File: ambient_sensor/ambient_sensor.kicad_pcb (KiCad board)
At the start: 2 copper layers, 69.5 x 54 mm, 25 parts, among them J1 Conn_01x02_Pin, J3 Conn_01x05_Pin, J4 Conn_01x01_Pin, J5 Conn_01x04_Pin, J6 Conn_01x02_Pin, U4 ATmega328-P, U6 LD1117S33TR_SOT223, Y1 Crystal

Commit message: no more errors
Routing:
- net +5V: track 223.2 -> 217.9 mm, vias 2 -> 3
- net unconnected-(U7-3V3-Pad2)_1: track 0.00 -> 2.50 mm
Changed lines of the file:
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@@
 	(net 30 "/MISO")
 	(net 31 "/DT")
-	(net 32 "unconnected-(U7-3V3-Pad2)")
-	(net 33 "unconnected-(U7-3V3-Pad2)_1")
-	(net 34 "unconnected-(U2-3V0-Pad4)")
-	(net 35 "unconnected-(U5-CTS-Pad2)")
+	(net 32 "unconnected-(U7-3V3-Pad2)_1")
+	(net 33 "unconnected-(U2-3V0-Pad4)")
+	(net 34 "unconnected-(U5-CTS-Pad2)")
 	(footprint "Resistor_SMD:R_1206_3216Metric"
 		(layer "F.Cu")
@@
 			(layers "*.Cu" "*.Mask")
 			(remove_unused_layers no)
-			(net 35 "unconnected-(U5-CTS-Pad2)")
+			(net 34 "unconnected-(U5-CTS-Pad2)")
 			(pinfunction "CTS")
 			(pintype "input")
@@
 			)
 		)
-		(fp_text user "MISO"
-			(at -37 -18.94144 0)
+		(fp_text user "Warning: unkown dimensions "
+			(at -7 -20 0)
 			(unlocked yes)
 			(layer "User.1")
 			(effects
 				(font
-					(size 0.93472 0.93472)
-					(thickness 0.08128)
+					(size 1 1)
+					(thickness 0.1)
 				)
 				(justify right bottom)
 			)
 		)
-		(fp_text user "3V3"
-			(at -37.801187 -6.24144 0)
+		(fp_text user "5V"
+			(at -38.691397 -8.78144 0)
 			(unlocked yes)
 			(layer "User.1")
@@
 			)
 		)
-		(fp_text user "GND"
-			(at -37.534126 -21.48144 0)
+		(fp_text user "SCK"
+			(at -37.623146 -16.40144 0)
 			(unlocked yes)
 			(layer "User.1")
@@
 			)
 		)
-		(fp_text user "MOSI"
-			(at -37 -13.86144 0)
+		(fp_text user "MISO"
+			(at -37 -18.94144 0)
 			(unlocked yes)
 			(layer "User.1")
@@
 			)
 		)
-		(fp_text user "GND"
-			(at -37.623146 -3.70144 0)
+		(fp_text user "3V3"
+			(at -37.801187 -6.24144 0)
 			(unlocked yes)
 			(layer "User.1")
@@
 			)
 		)
-		(fp_text user "5V"
-			(at -38.691397 -8.78144 0)
+		(fp_text user "MOSI"
+			(at -37 -13.86144 0)
 			(unlocked yes)
 			(layer "User.1")
@@
 			)
 		)
-		(fp_text user "Warning: unkown dimensions "
-			(at -7 -20 0)
+		(fp_text user "GND"
+			(at -37.534126 -21.48144 0)
 			(unlocked yes)
 			(layer "User.1")
 			(effects
 				(font
-					(size 1 1)
-					(thickness 0.1)
+					(size 0.93472 0.93472)
+					(thickness 0.08128)
 				)
 				(justify right bottom)
 			)
 		)
-		(fp_text user "CS"
-			(at -38.557866 -11.32144 0)
+		(fp_text user "GND"
+			(at -37.623146 -3.70144 0)
 			(unlocked yes)
 			(layer "User.1")
@@
 			)
 		)
-		(fp_text user "SCK"
-			(at -37.623146 -16.40144 0)
+		(fp_text user "CS"
+			(at -38.557866 -11.32144 0)
 			(unlocked yes)
 			(layer "User.1")
@@
 			(layer "User.4")
 			(pts
-				(xy 225.25 139.25) (xy 225.25 146.5)
+				(xy 226.611 119.979) (xy 226.611 137.759)
 			)
-			(height 23)
-			(gr_text "7.2500 mm"
-				(at 201.15 142.875 90)
+			(height 7.861)
+			(gr_text "17.7800 mm"
+				(at 217.6 128.869 90)
 				(layer "User.4")
 				(effects
 					(font
 						(size 1 1)
-						(thickness 0.1)
+						(thickness 0.15)
 					)
 				)
@@
 			(layer "User.4")
 			(pts
-				(xy 226.611 119.979) (xy 229.111 119.979)
+				(xy 225.25 139.25) (xy 225.25 146.5)
 			)
-			(height -13.479)
-			(gr_text "2.5000 mm"
-				(at 227.861 105.4 0)
+			(height 23)
+			(gr_text "7.2500 mm"
+				(at 201.15 142.875 90)
 				(layer "User.4")
 				(effects
@@
 			(layer "User.4")
 			(pts
-				(xy 226.611 119.979) (xy 226.611 137.759)
+				(xy 226.611 119.979) (xy 229.111 119.979)
 			)
-			(height 7.861)
-			(gr_text "17.7800 mm"
-				(at 217.6 128.869 90)
+			(height -13.479)
+			(gr_text "2.5000 mm"
+				(at 227.861 105.4 0)
 				(layer "User.4")
 				(effects
 					(font
 						(size 1 1)
-						(thickness 0.15)
+						(thickness 0.1)
 					)
 				)
@@
 			(remove_unused_layers no)
 		)
-		(pad "" thru_hole circle
-			(at -44 0)
-			(size 3 3)
-			(drill 2)
-			(layers "*.Cu" "*.Mask")
-			(remove_unused_layers no)
-		)
 		(pad "1" thru_hole roundrect
 			(at -44.389 -3.991 180)
@@
 			(chamfer_ratio 0.2928932188)
 			(chamfer top_left top_right bottom_left bottom_right)
-			(net 33 "unconnected-(U7-3V3-Pad2)_1")
+			(net 32 "unconnected-(U7-3V3-Pad2)_1")
 			(pinfunction "3V3")
 			(pintype "power_in+no_connect")
@@
 			(chamfer_ratio 0.2928932188)
 			(chamfer top_left top_right bottom_left bottom_right)
-			(net 32 "unconnected-(U7-3V3-Pad2)")
+			(net 32 "unconnected-(U7-3V3-Pad2)_1")
 			(pinfunction "3V3")
 			(pintype "power_in+no_connect")
@@
 			(layers "*.Cu" "*.Mask")
 			(remove_unused_layers no)
-			(net 34 "unconnected-(U2-3V0-Pad4)")
+			(net 33 "unconnected-(U2-3V0-Pad4)")
 			(pinfunction "3V0")
 			(pintype "power_in+no_connect")
@@
 	)
 	(segment
+		(start 199.75 135.25)
+		(end 198.25 135.25)
+		(width 0.5)
+		(layer "F.Cu")
+		(net 15)
+	)
+	(segment
 		(start 196.75 133.75)
 		(end 184 133.75)
@@
 	)
 	(segment
+		(start 205.25 140.75)
+		(end 199.75 135.25)
+		(width 0.5)
+		(layer "F.Cu")
+		(net 15)
+	)
+	(segment
 		(start 177.175 118.65)
 		(end 176.525 118.65)
@@
 		(net 15)
 	)
+	(via
+		(at 205.25 140.75)
+		(size 1.524)
+		(drill 0.5)
+		(layers "F.Cu" "B.Cu")
+		(net 15)
+	)
 	(segment
 		(start 185.275 122)
@@
 	)
 	(segment
-		(start 231 116.25)
-		(end 231 130.79)
+		(start 225.2 134)
+		(end 225.29 134)
+		(width 0.5)
+		(layer "B.Cu")
+		(net 15)
+	)
+	(segment
+		(start 177.145 119.645)
+		(end 181.5 124)
+		(width 0.5)
+		(layer "B.Cu")
+		(net 15)
+	)
+	(segment
+		(start 177.145 113.75)
+		(end 177.145 119.645)
 		(width 0.5)
 		(layer "B.Cu")
@@
 	)
 	(segment
-		(start 231 130.79)
-		(end 229.111 132.679)
+		(start 184.88 136.5)
+		(end 187.13 138.75)
 		(width 0.5)
 		(layer "B.Cu")
@@
 	)
 	(segment
-		(start 191.285 106.26)
-		(end 189.775 104.75)
+		(start 225.29 134)
+		(end 226.611 132.679)
 		(width 0.5)
 		(layer "B.Cu")
@@
 	)
 	(segment
-		(start 191.285 108.75)
-		(end 191.285 106.26)
+		(start 225.2 136.8)
+		(end 225.2 134)
 		(width 0.5)
 		(layer "B.Cu")
@@
 	)
 	(segment
-		(start 177.145 129.895)
-		(end 183.75 136.5)
+		(start 181.5 124)
+		(end 181.5 134.25)
+		(width 0.5)
+		(layer "B.Cu")
+		(net 15)
+	)
+	(segment
+		(start 191.285 106.26)
+		(end 189.775 104.75)
+		(width 0.5)
+		(layer "B.Cu")
+		(net 15)
+	)
+	(segment
+		(start 191.285 108.75)
+		(end 191.285 106.26)
 		(width 0.5)
 		(layer "B.Cu")
@@
 	)
 	(segment
-		(start 177.145 113.75)
-		(end 177.145 129.895)
+		(start 221.25 140.75)
+		(end 225.2 136.8)
 		(width 0.5)
 		(layer "B.Cu")
@@
 	)
 	(segment
-		(start 183.75 136.5)
-		(end 184.88 136.5)
-		(width 0.5)
-		(layer "B.Cu")
-		(net 15)
-	)
-	(segment
 		(start 176.595 106.93)
 		(end 176.595 108.78)
@@
 	)
 	(segment
-		(start 184.88 136.5)
-		(end 187.13 138.75)
+		(start 187 122)
+		(end 188 123)
 		(width 0.5)
 		(layer "B.Cu")
@@
 	)
 	(segment
-		(start 187 122)
-		(end 188 123)
+		(start 227.361 132.679)
+		(end 229.861 132.679)
 		(width 0.5)
 		(layer "B.Cu")
@@
 	)
 	(segment
-		(start 227.361 132.679)
-		(end 229.861 132.679)
+		(start 181.5 134.25)
+		(end 183.75 136.5)
 		(width 0.5)
 		(layer "B.Cu")
@@
 	)
 	(segment
-		(start 202.25 135.25)
-		(end 204.015 133.485)
+		(start 183.75 136.5)
+		(end 184.88 136.5)
 		(width 0.5)
 		(layer "B.Cu")
@@
 	)
 	(segment
-		(start 209.095 120.18)
-		(end 206.555 120.18)
+		(start 202.25 135.25)
+		(end 204.015 133.485)
 		(width 0.5)
 		(layer "B.Cu")
@@
 	)
 	(segment
-		(start 209.095 111.94)
-		(end 209.095 120.18)
+		(start 209.095 120.18)
+		(end 206.555 120.18)
 		(width 0.5)
 		(layer "B.Cu")
@@
 	(segment
 		(start 209.095 111.94)
-		(end 226.69 111.94)
-		(width 0.5)
-		(layer "B.Cu")
-		(net 15)
-	)
-	(segment
-		(start 226.69 111.94)
-		(end 231 116.25)
+		(end 209.095 120.18)
 		(width 0.5)
 		(layer "B.Cu")
@@
 	)
 	(segment
+		(start 221.25 140.75)
+		(end 205.25 140.75)
+		(width 0.5)
+		(layer "B.Cu")
+		(net 15)
+	)
+	(segment
 		(start 177.145 113.75)
 		(end 177.145 114.5)
@@
 	)
 	(segment
-		(start 199 139.25)
+		(start 223.75 135.5)
+		(end 223.75 133)
+		(width 0.5)
+		(layer "B.Cu")
+		(net 31)
+	)
+	(segment
+		(start 196.395 127.8)
 		(end 196.395 136.645)
 		(width 0.5)
@@
 	)
 	(segment
-		(start 196.395 136.645)
-		(end 196.395 127.8)
+		(start 229.861 130.139)
+		(end 227.361 130.139)
 		(width 0.5)
 		(layer "B.Cu")
@@
 	(segment
 		(start 220 139.25)
-		(end 199 139.25)
+		(end 223.75 135.5)
 		(width 0.5)
 		(layer "B.Cu")
@@
 	)
 	(segment
-		(start 229.861 130.139)
-		(end 227.361 130.139)
+		(start 223.75 133)
+		(end 226.611 130.139)
 		(width 0.5)
 		(layer "B.Cu")
@@
 	)
 	(segment
-		(start 224.5 134.75)
-		(end 224.5 132.25)
+		(start 196.395 136.645)
+		(end 199 139.25)
 		(width 0.5)
 		(layer "B.Cu")
@@
 	)
 	(segment
-		(start 224.5 134.75)
+		(start 199 139.25)
 		(end 220 139.25)
 		(width 0.5)
@@
 	)
 	(segment
-		(start 224.5 132.25)
-		(end 226.611 130.139)
+		(start 226.611 135.219)
+		(end 229.111 135.219)
 		(width 0.5)
 		(layer "B.Cu")
-		(net 31)
+		(net 32)
 	)
 	(zone

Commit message: organizing
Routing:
- net +5V: track 217.9 -> 207.6 mm

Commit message: battery case
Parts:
- added REF**: battery_case, sensors:battery_case, F.Cu at (106.2, 145.8)
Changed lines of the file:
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@@
+		)
+	)
+	(footprint "sensors:battery_case"
+		(layer "F.Cu")
+		(at 106.25 145.75)
+		(property "Reference" "REF**"
+			(at 0 -0.5 0)
+			(unlocked yes)
+			(layer "F.SilkS")
+			(hide yes)
+			(effects
+				(font
+					(size 1 1)
+					(thickness 0.1)
+				)
+			)
+		)
+		(property "Value" "battery_case"
+			(at 0 1 0)
+			(unlocked yes)
+			(layer "F.Fab")
+			(hide yes)
+			(effects
+				(font
+					(size 1 1)
+					(thickness 0.15)
+				)
+			)
+		)
+		(property "Footprint" "sensors:battery_case"
+			(at 0 0 0)
+			(unlocked yes)
+			(layer "F.Fab")
+			(hide yes)
+			(effects
+				(font
+					(size 1 1)
+					(thickness 0.15)
+				)
+			)
+		)
+		(property "Datasheet" ""
+			(at 0 0 0)
+			(unlocked yes)
+			(layer "F.Fab")
+			(hide yes)
+			(effects
+				(font
+					(size 1 1)
+					(thickness 0.15)
+				)
+			)
+		)
+		(property "Description" ""
+			(at 0 0 0)
+			(unlocked yes)
+			(layer "F.Fab")
+			(hide yes)
+			(effects
+				(font
+					(size 1 1)
+					(thickness 0.15)
+				)
+			)
+		)
+		(attr smd board_only)
+		(fp_rect
+			(start -0.25 -50.75)
+			(end 52.75 -0.75)
+			(stroke
+				(width 0.1)
+				(type default)
+			)
+			(fill none)
+			(layer "F.CrtYd")
+		)
+		(fp_text user "4 AAA 1.5V"
+			(at 5.75 -25.5 0)
+			(unlocked yes)
+			(layer "Cmts.User")
+			(effects
+				(font
+					(size 5 5)
+					(thickness 0.2)
+				)
+				(justify left bottom)
+			)
+		)
+		(fp_text user "Battery case"
+			(at 3 -19.75 0)
+			(unlocked yes)
+			(layer "Cmts.User")
+			(effects
+				(font
+					(size 5 5)
+					(thickness 0.2)
+				)
+				(justify left bottom)
+			)
 		)
 	)

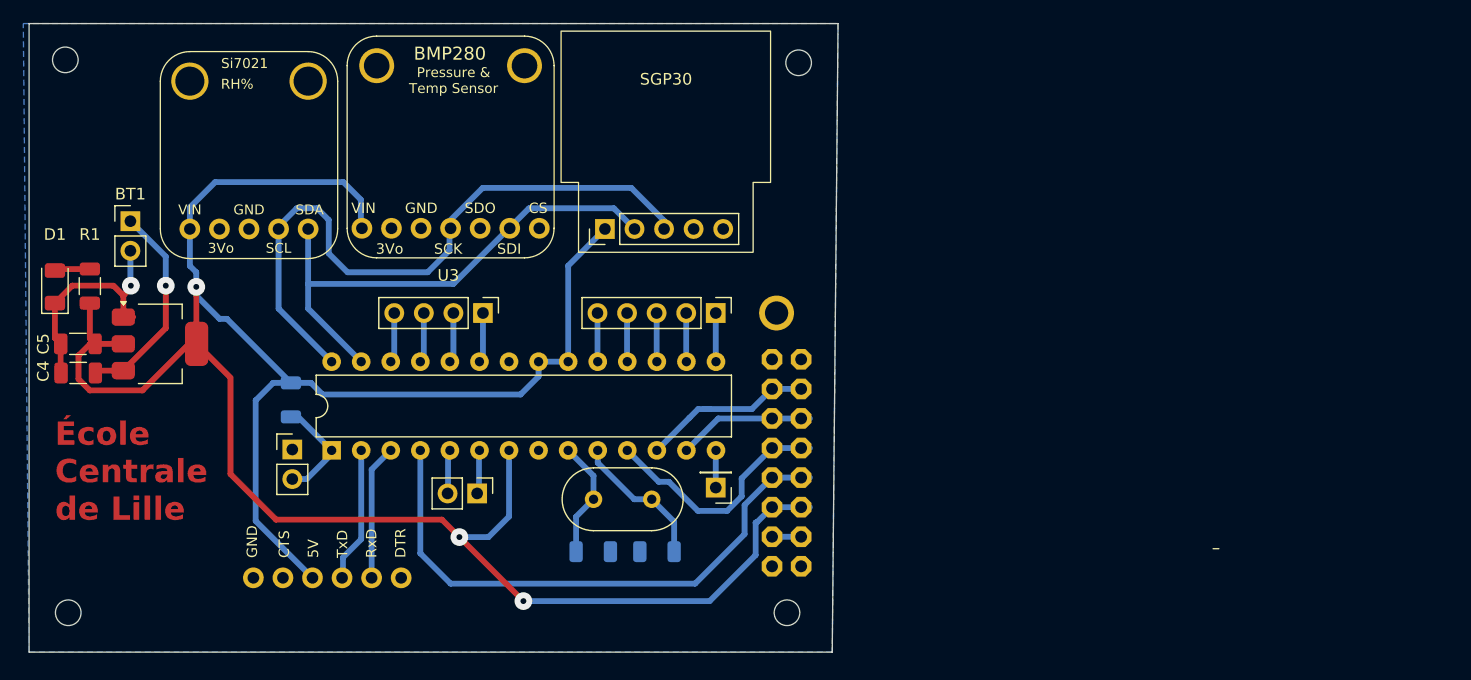
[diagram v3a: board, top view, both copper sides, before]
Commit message: bluetooth module created
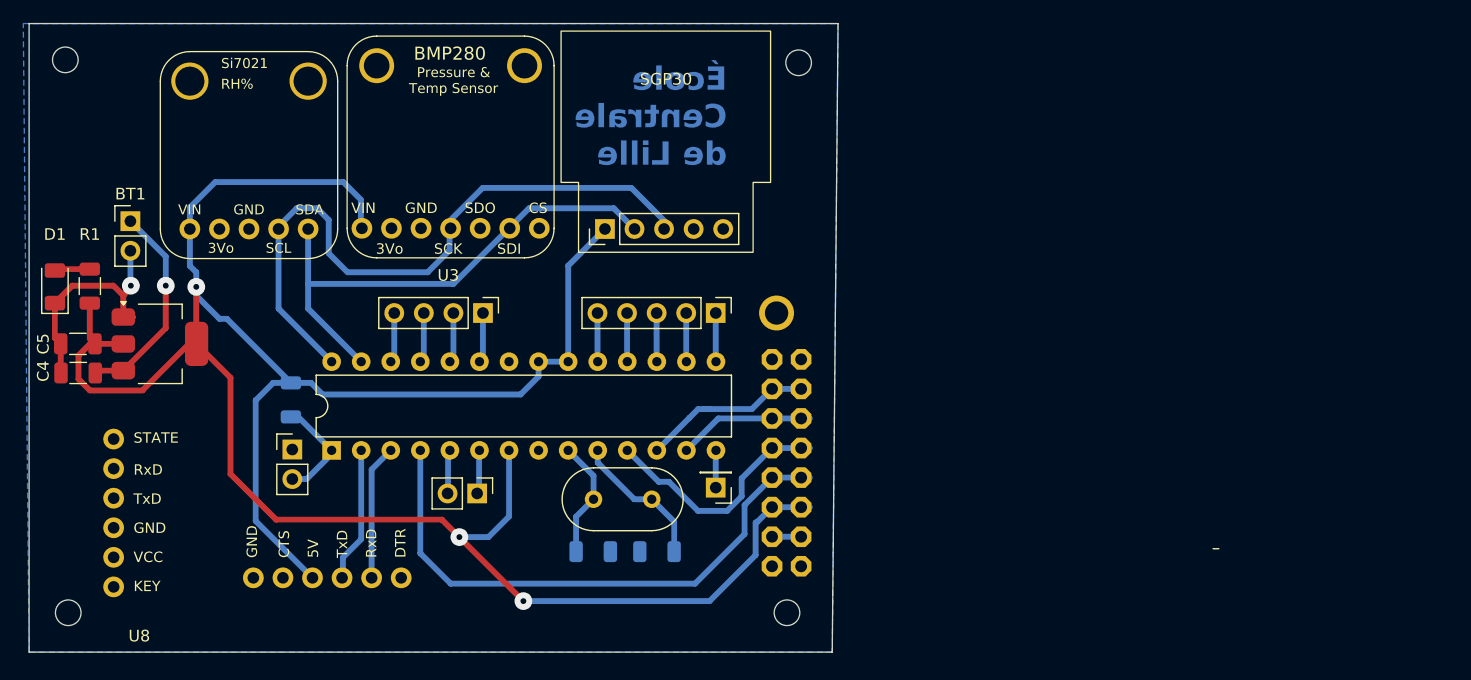
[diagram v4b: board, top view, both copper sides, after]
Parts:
- added U8: ~, sensors:HC-05_breakboard, F.Cu at (172.2, 144.2)
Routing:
- net unconnected-(U7-3V3-Pad2)_1: track 0.00 -> 2.50 mm
- net unconnected-(U7-3V3-Pad2): track 2.50 -> 0.00 mm

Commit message: rudimentary bluetooth
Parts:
- moved U8 65.0 mm to (230.7, 115.8)
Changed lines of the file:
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@@
 	(footprint "sensors:HC-05_breakboard"
 		(layer "F.Cu")
-		(at 172.25 144.25)
+		(at 230.704 115.842)
 		(property "Reference" "U8"
 			(at 0 -0.5 0)

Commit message: before impleenting the changes
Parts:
- added D2: LED, LED_SMD:LED_1206_3216Metric, F.Cu at (208.5, 116.0)
- added R3: 1k, Resistor_SMD:R_1206_3216Metric, B.Cu at (205.0, 116.0)
- R1: value 120 -> 1k
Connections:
- net Net-(J5-Pin_1) renamed /LED_BUILTIN
- J3 pad 1: Net-(J3-Pin_1) -> /RxS
- J3 pad 5: Net-(J3-Pin_5) -> /CLK
- J4 pad 1: Net-(J4-Pin_1) -> /TxS
- U4 pad 13: /CLK -> unconnected-(U4-PD7-Pad13)
- U4 pad 14: Net-(J4-Pin_1) -> /TxS
- U4 pad 15: Net-(J3-Pin_1) -> /RxS
- U4 pad 19: Net-(J3-Pin_5) -> /CLK
- U8 pad 2: unconnected-(U8-RxD-Pad2) -> /TxS
- U8 pad 3: unconnected-(U8-TxD-Pad3) -> /RxS
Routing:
- net Net-(D2-A): track 0.00 -> 10.4 mm, vias 0 -> 1
- net GND: track 20.5 -> 26.1 mm, vias 1 -> 2
- net Net-(J3-Pin_5): track 4.19 -> 0.00 mm
- net Net-(J3-Pin_1): track 4.19 -> 0.00 mm
- net /RxS: track 0.00 -> 4.19 mm
- net /CLK: track 11.7 -> 15.9 mm
- net /LED_BUILTIN: track 3.80 -> 7.64 mm
- net Net-(J4-Pin_1): track 3.21 -> 0.00 mm
- net /TxS: track 0.00 -> 3.21 mm
